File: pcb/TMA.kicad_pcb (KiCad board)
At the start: 2 copper layers, 18 x 18 mm, 22 parts, among them J1 Conn_01x02, J2 Conn_01x05, J3 Conn_01x04, J4 Conn_01x02, U1 BMP280, U2 BMI160, U3 ATtiny1614-SS, U4 MIC5504-3.3YM5

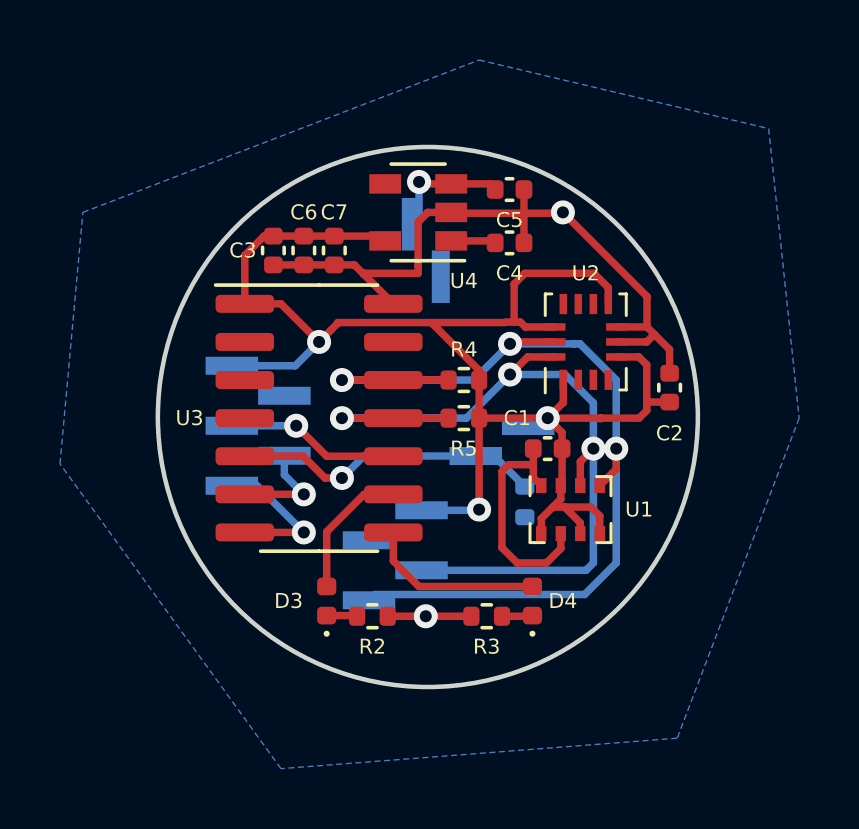
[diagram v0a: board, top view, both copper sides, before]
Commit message: fix lipo connection, move R1 to front
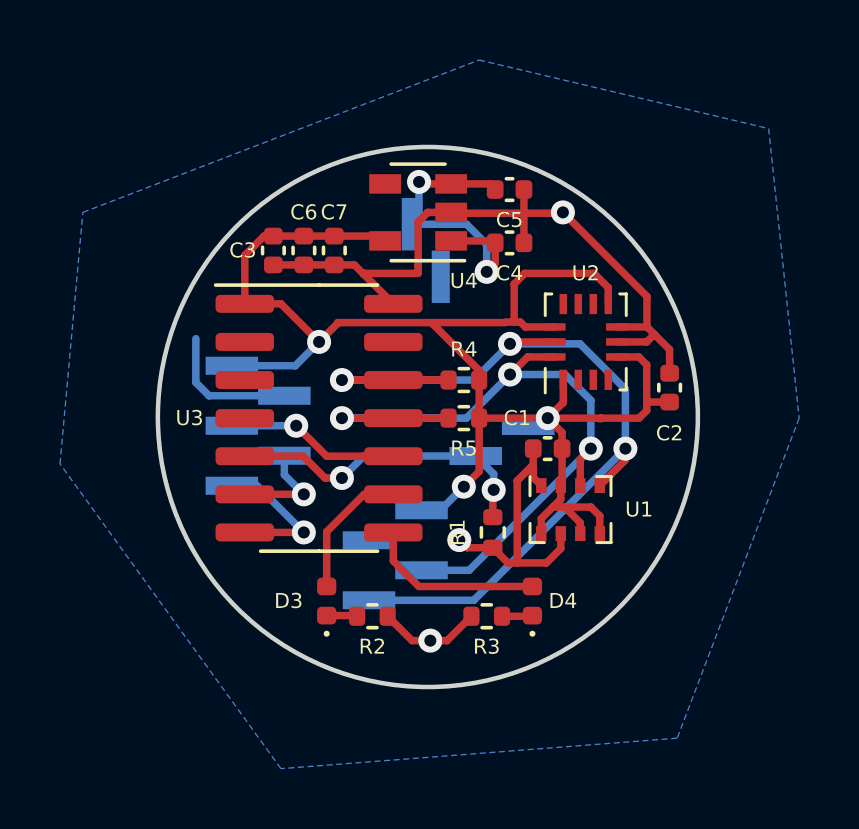
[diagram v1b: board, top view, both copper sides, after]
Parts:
- R1: moved to F.Cu
- moved R1 1.47 mm to (77.2, 53.8)
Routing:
- net GND: track 34.8 -> 41.4 mm, vias 2 -> 3
- net Net-(C4-Pad1): track 5.66 -> 10.5 mm, vias 1 -> 2
- net SDA: track 27.3 -> 24.9 mm
- net SCL: track 31.5 -> 29.9 mm
- net +3V3: track 54.4 -> 53.7 mm
- net MODE: track 10.4 -> 10.6 mm, vias 1 -> 2
